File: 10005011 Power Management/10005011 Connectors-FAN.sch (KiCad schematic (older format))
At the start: 63 parts, among them IC25 L78M24CDT, IC6 TLV3012AIDBV, J10 BATTERY, J6 FAN, J7 CPU BOARD, J9 BLOWER, T23 IRLML2803, T31 IRLML5103

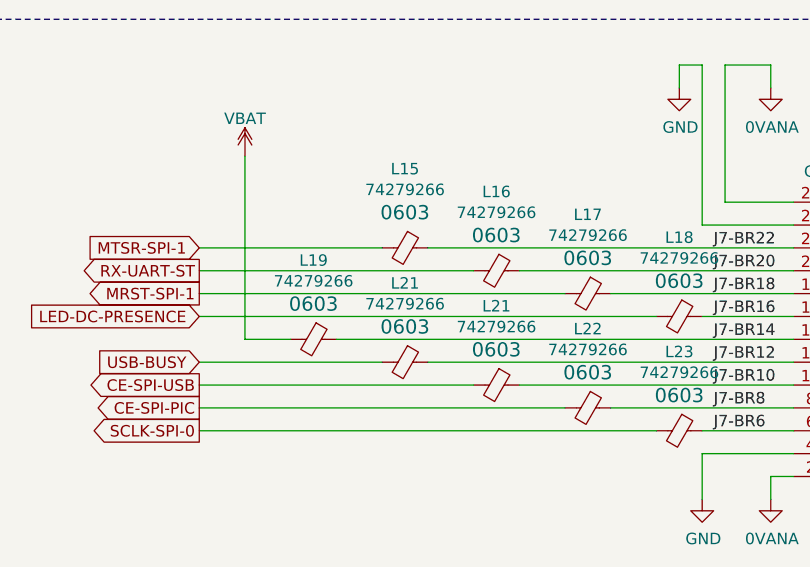
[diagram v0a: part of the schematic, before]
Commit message: solved repeated Res and Ind
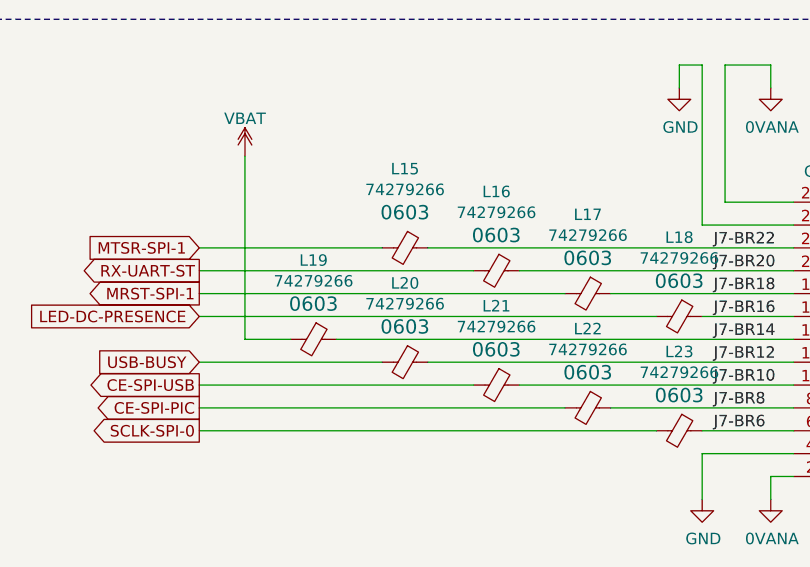
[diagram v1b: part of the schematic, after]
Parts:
- renumbered L21 to L20
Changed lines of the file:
@@
 $EndComp
 $Comp
-L 10005011_Power_Management_Schematic_Symbols:74279266 L21
+L 10005011_Power_Management_Schematic_Symbols:74279266 L20
 U 1 1 5EA74223
 P 6950 2850
-F 0 "L21" V 6605 2850 50  0000 C CNN
+F 0 "L20" V 6605 2850 50  0000 C CNN
 F 1 "74279266" V 6696 2850 50  0000 C CNN
 F 2 "10005011 Power Management:C0603_1" V 6880 2850 50  0001 C CNN

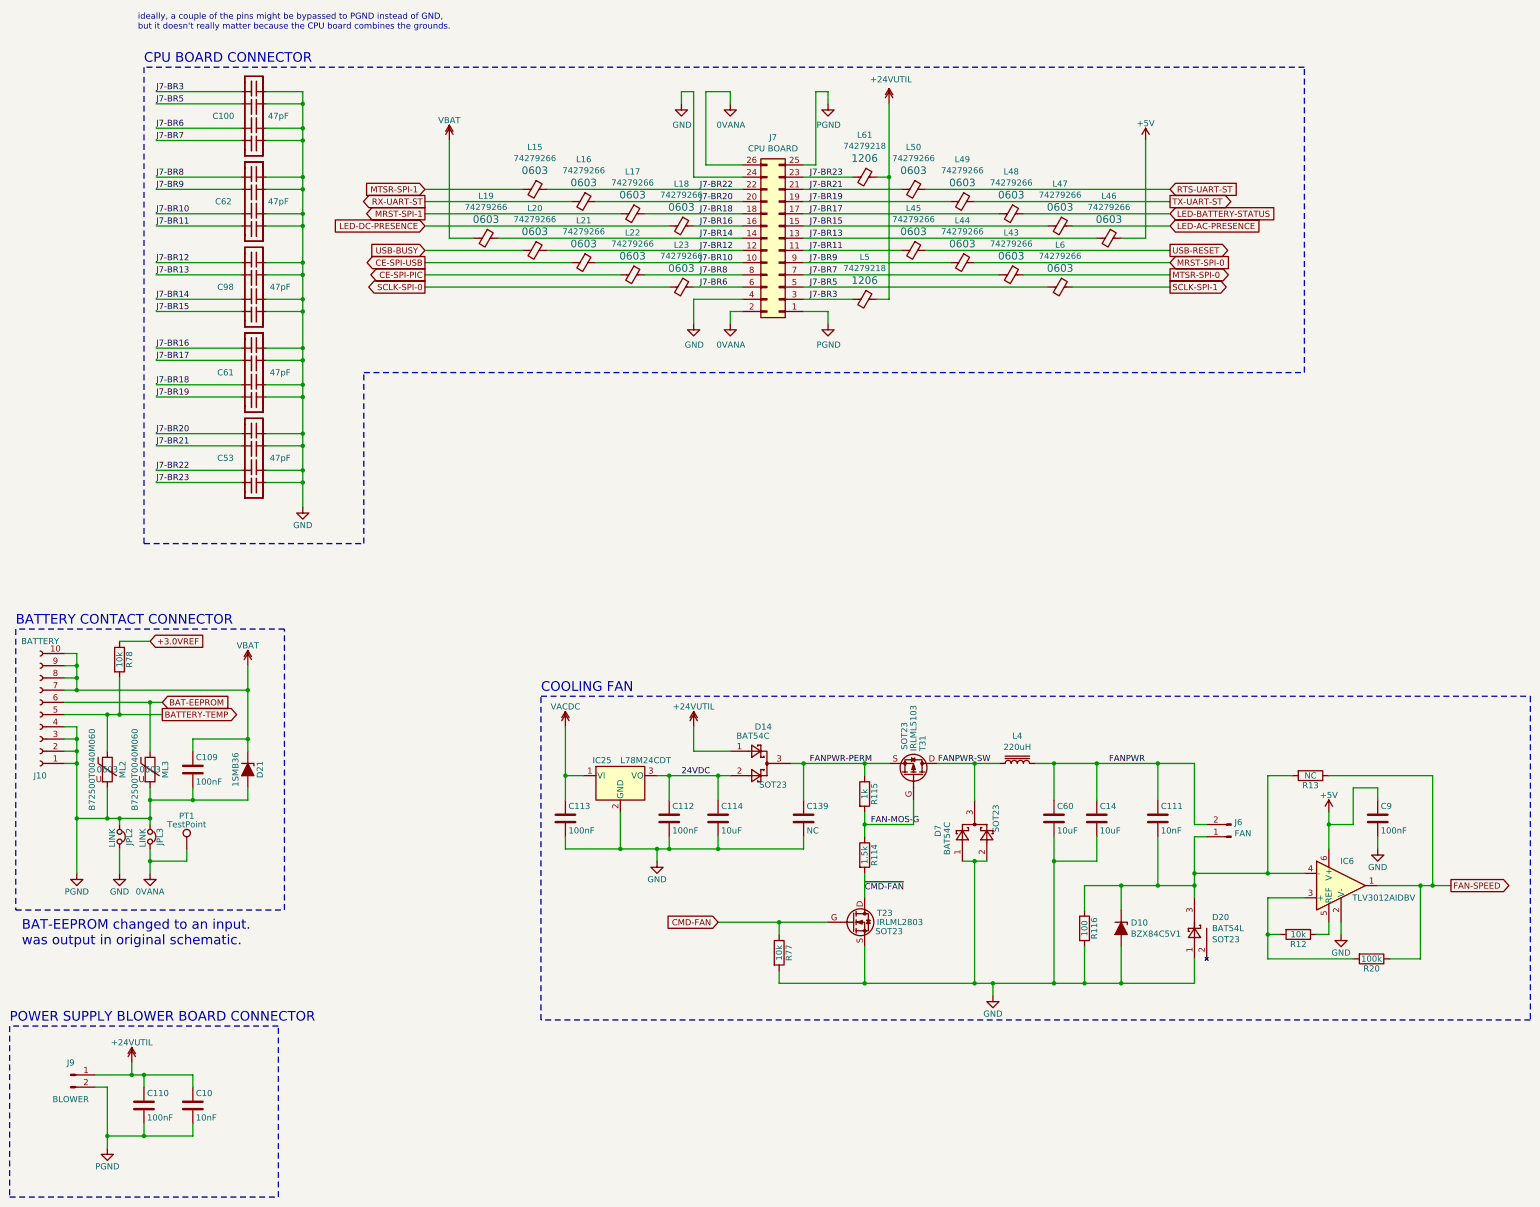
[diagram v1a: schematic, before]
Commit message: Powermanagement dev sheet4
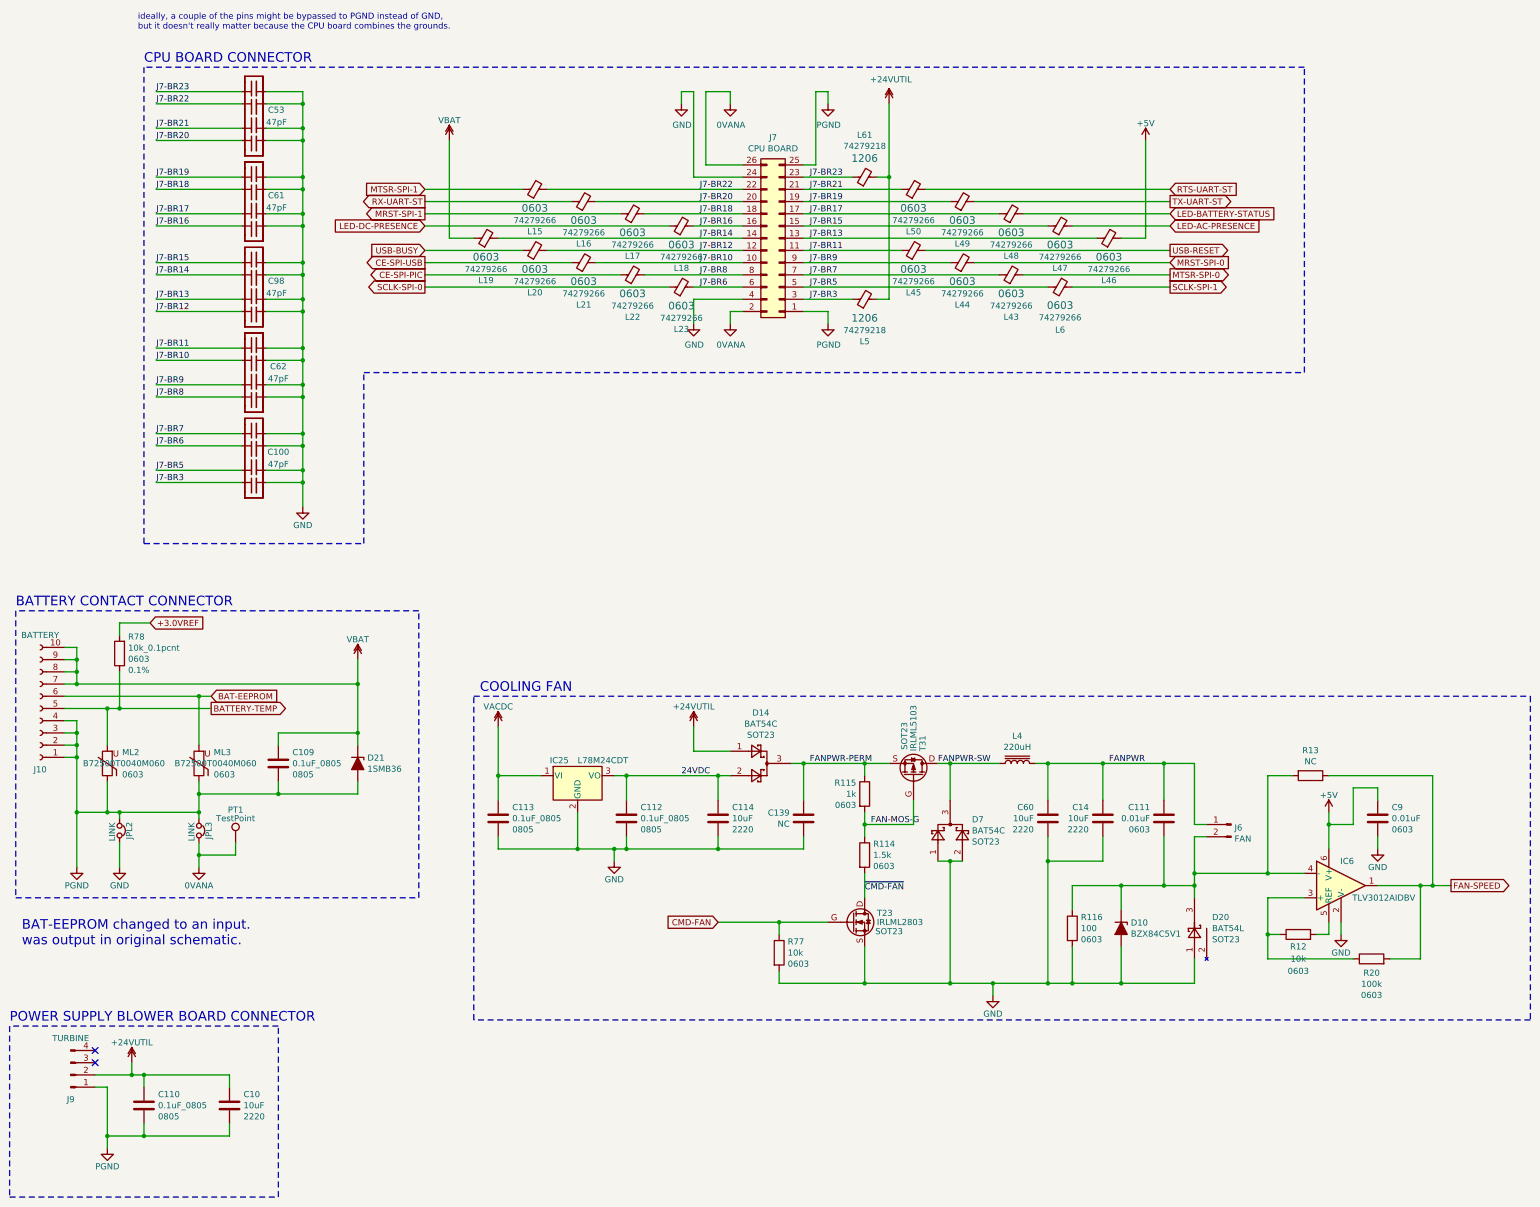
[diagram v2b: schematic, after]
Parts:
- removed C10: 10nF, 10005011 Power Management:C2220_1, symbol Device:C
- removed C109, C110, C112, C113: 100nF, 10005011 Power Management:C0805_1, symbol Device:C
- removed C111: 10nF, 10005011 Power Management:C0603_1, symbol Device:C
- removed C114, C14, C60: 10uF, 10005011 Power Management:C2220_1, symbol Device:C
- removed C9: 100nF, 10005011 Power Management:C0402_1, symbol Device:C
- removed J9: BLOWER, 10005011 Power Management:MOL43650-02D_1, symbol Connector:Conn_01x02_Male
- removed R114: 1.5k, 10005011 Power Management:RC1206_1, symbol Device:R
- removed R115: 1k, 10005011 Power Management:RC1206_1, symbol Device:R
- removed R116: 100, 10005011 Power Management:RC1206_1, symbol Device:R
- removed R12, R77, R78: 10k, 10005011 Power Management:R0603_1, symbol Device:R
- removed R20: 100k, 10005011 Power Management:R0603_1, symbol Device:R
- added C10, C114, C14, C60: 10uF, Capacitor_SMD:C_2220_5650Metric, symbol 10005011_Power_Management_Schematic_Symbols:10uF
- added C109, C110, C112, C113: 0.1uF_0805, Capacitor_SMD:C_0805_2012Metric, symbol 10005011_Power_Management_Schematic_Symbols:0.1uF_0805
- added C111, C9: 0.01uF, Capacitor_SMD:C_0603_1608Metric, symbol 10005011_Power_Management_Schematic_Symbols:0.01uF
- added J9: TURBINE, symbol Connector:Conn_01x04_Male
- added R114: 1.5k, Resistor_SMD:R_0603_1608Metric, symbol 10005011_Power_Management_Schematic_Symbols:1.5k
- added R115: 1k, Resistor_SMD:R_0603_1608Metric, symbol 10005011_Power_Management_Schematic_Symbols:1k
- added R116: 100, Resistor_SMD:R_0603_1608Metric, symbol 10005011_Power_Management_Schematic_Symbols:100
- added R12, R77: 10k, Resistor_SMD:R_0603_1608Metric, symbol 10005011_Power_Management_Schematic_Symbols:10k
- added R20: 100k, Resistor_SMD:R_0603_1608Metric, symbol 10005011_Power_Management_Schematic_Symbols:100k
- added R78: 10k_0.1pcnt, Resistor_SMD:R_0603_1608Metric, symbol 10005011_Power_Management_Schematic_Symbols:10k_0.1pcnt
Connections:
- net +24VUTIL: now also L5.2, L61.2, C10.2, C110.2, J9.2 (Pin_2); no longer L5.1, L61.1
- net +3.0VREF: now also R78.2
- net +5V: now also L46.2, C9.1; no longer L46.1
- net 24VDC: now also C112.2, C114.2
- net BAT-EEPROM: now also ML3.2; no longer ML3.1
- net BATTERY-TEMP: now also ML2.2, R78.1; no longer ML2.1
- net CE-SPI-PIC: now also L22.1; no longer L22.2
- net CE-SPI-USB: now also L21.1; no longer L21.2
- net CMD-FAN: now also R77.1
- net FAN-MOS-G: now also R114.1, R115.2
- net FAN-SPEED: now also R20.2
- net FANPWR: now also J6.1 (Pin_1), C111.2, C14.2, C60.2; no longer J6.2 (Pin_2)
- net FANPWR-PERM: now also C139.2, R115.1; no longer C139.1
- net GND: now also C100.1, C100.2, C100.3, C100.4, C139.1, C53.1, C53.2, C53.3, C53.4, C61.1, C61.2, C61.3, C61.4, C62.1, C62.2, C62.3, C62.4, C98.1, C98.2, C98.3, C98.4, C112.1, C113.1, C114.1, C14.1, C60.1, C9.2, R116.2, R77.2; no longer C100.5, C100.6, C100.7, C100.8, C139.2, C53.5, C53.6, C53.7, C53.8, C61.5, C61.6, C61.7, C61.8, C62.5, C62.6, C62.7, C62.8, C98.5, C98.6, C98.7, C98.8
- net J7-BR10: now also C62.6, L21.2; no longer C62.3, L21.1
- net J7-BR11: now also C62.5, L45.1; no longer C62.4, L45.2
- net J7-BR12: now also C98.8, L20.2; no longer C98.1, L20.1
- net J7-BR13: now also C98.7, L46.1; no longer C98.2, L46.2
- net J7-BR14: now also C98.6, L19.2; no longer C98.3, L19.1
- net J7-BR15: now also C98.5, L47.1; no longer C98.4, L47.2
- net J7-BR16: now also C61.8, L18.2; no longer C61.1, L18.1
- net J7-BR17: now also C61.7, L48.1; no longer C61.2, L48.2
- net J7-BR18: now also C61.6, L17.2; no longer C61.3, L17.1
- net J7-BR19: now also C61.5, L49.1; no longer C61.4, L49.2
- net J7-BR20: now also C53.8, L16.2; no longer C53.1, L16.1
- net J7-BR21: now also C53.7, L50.1; no longer C53.2, L50.2
- net J7-BR22: now also C53.6, L15.2; no longer C53.3, L15.1
- net J7-BR23: now also C53.5, L61.1; no longer C53.4, L61.2
- net J7-BR3: now also C100.8, L5.1; no longer C100.1, L5.2
- net J7-BR5: now also C100.7; no longer C100.2
- net J7-BR6: now also C100.6, L23.2; no longer C100.3, L23.1
- net J7-BR7: now also C100.5, L43.1; no longer C100.4, L43.2
- net J7-BR8: now also C62.8, L22.2; no longer C62.1, L22.1
- net J7-BR9: now also C62.7, L44.1; no longer C62.2, L44.2
- net LED-AC-PRESENCE: now also L47.2; no longer L47.1
- net LED-BATTERY-STATUS: now also L48.2; no longer L48.1
- net LED-DC-PRESENCE: now also L18.1; no longer L18.2
- net MRST-SPI-0: now also L44.2; no longer L44.1
- net MRST-SPI-1: now also L17.1; no longer L17.2
- net MTSR-SPI-0: now also L43.2; no longer L43.1
- net MTSR-SPI-1: now also L15.1; no longer L15.2
- net PGND: now also ML2.1, ML3.1, C10.1, C109.1, C110.1, J9.1 (Pin_1); no longer ML2.2, ML3.2
- net RTS-UART-ST: now also L50.2; no longer L50.1
- net RX-UART-ST: now also L16.1; no longer L16.2
- net SCLK-SPI-0: now also L23.1; no longer L23.2
- net TX-UART-ST: now also L49.2; no longer L49.1
- net USB-BUSY: now also L20.1; no longer L20.2
- net USB-RESET: now also L45.2; no longer L45.1
- net VACDC: now also C113.2
- net VBAT: now also L19.1, C109.2; no longer L19.2
- net ~CMD-FAN: now also R114.2
- net at IC6.3 (+): now also R12.1, R20.1
- net at D10.K, D20.3, IC6.4 (-)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: now also J6.2 (Pin_2), C111.1, R116.1; no longer J6.1 (Pin_1)
- net at IC6.5 (REF): now also R12.2
- no-connect marks 0 -> 2
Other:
- moved on the sheet: C100, C53, C61, C62, D21, D7, IC25, J10, JPL2, JPL3, ML2, ML3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

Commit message: Powermanagement dev netlist fix
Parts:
- J9: footprint (none) -> 10005011 Power Management:MOL43650-02D_1; Description (none) -> CONNECTOR MICRO-FIT, 2 CIRCUITS,3MM,5A,250V; Item Number (none) -> 10022874; Manufacturer (none) -> MOLEX; Manufacturer_No (none) -> 43650-0224
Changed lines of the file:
@@
 F 0 "J9" H 3150 9800 50  0000 C CNN
 F 1 "TURBINE" H 3150 9300 50  0000 C CNN
-F 2 "" H 3150 9600 50  0001 C CNN
+F 2 "10005011 Power Management:MOL43650-02D_1" H 3150 9600 50  0001 C CNN
 F 3 "~" H 3150 9600 50  0001 C CNN
+F 4 "CONNECTOR MICRO-FIT, 2 CIRCUITS,3MM,5A,250V" H 3150 9600 50  0001 C CNN "Description"
+F 5 "10022874" H 3150 9600 50  0001 C CNN "Item Number"
+F 6 "MOLEX" H 3150 9600 50  0001 C CNN "Manufacturer"
+F 7 "43650-0224" H 3150 9600 50  0001 C CNN "Manufacturer_No"
 	1    3150 9600
 	1    0    0    1

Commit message: Powermanagement dev library
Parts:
- C10, C114, C14, C60: footprint Capacitor_SMD:C_2220_5650Metric -> 10005011 Power Management:C2220_1; symbol 10005011_Power_Management_Schematic_Symbols:10uF -> Device:C; Bom_Footprint 2220 -> (none); Description CAP CER 10UF 50V X7R 2220 -> CAPACITOR CERAMIC, 10UF,+/-10%,50V; Item Number (none) -> 10039581; Manufacturer (none) -> AVX; Manufacturer_No (none) -> 22205C106K4Z4A
- C100, C61, C62, C98: symbol 10005011_Power_Management_Schematic_Symbols:47pF_array -> 10005011_Power_Management:47pF_array; Description CAP ARRAY 47PF 50V NP0 0612 -> CAPACITOR ARRAY, 47PF, 50V, +/-10%,NPO,0612; Dielectric NPO -> (none); Item Number (none) -> 10022136; Notes Need to create a footprint -> (none); Voltage 50V -> (none)
- C109, C110, C112, C113: value 0.1uF_0805 -> 100nF; footprint Capacitor_SMD:C_0805_2012Metric -> 10005011 Power Management:C0805_1; symbol 10005011_Power_Management_Schematic_Symbols:0.1uF_0805 -> Device:C; Bom_Footprint 0805 -> (none); Description CAP CER 0.1UF 50V X7R 0805 -> CAPACITOR CERAMIC, 100NF, +/-10%, 50V, X7R,0805; Item Number (none) -> 10022135
- C111, C9: footprint Capacitor_SMD:C_0603_1608Metric -> 10005011 Power Management:C0603_1; symbol 10005011_Power_Management_Schematic_Symbols:0.01uF -> Device:C
- C53: symbol 10005011_Power_Management_Schematic_Symbols:47pF_array -> 10005011_Power_Management:47pF_array; Description CAP ARRAY 47PF 50V NP0 0612 -> CAPACITOR ARRAY, 47PF, 50V, +/-10%,NPO,0612; Item Number (none) -> 10022136
- D10: symbol 10005011_Power_Management_Schematic_Symbols:BZX84C5V1 -> 10005011_Power_Management:BZX84C5V1; Description DIODE ZENER 5.1V 300MW SOT23-3 -> DIODE ZENER, 0.35,5.1V, SOT23; Item Number (none) -> 10022657
- D14, D7: symbol 10005011_Power_Management_Schematic_Symbols:BAT54C -> 10005011_Power_Management:BAT54C; BOM_Footprint SOT23 -> (none); Item Number (none) -> 10022653
- D20: value BAT54L -> BAT54; symbol 10005011_Power_Management_Schematic_Symbols:BAT54L -> 10005011_Power_Management:BAT54; BOM_Footprint SOT23 -> (none); Item Number (none) -> 10022652
- D21: symbol 10005011_Power_Management_Schematic_Symbols:SZ1SMB -> 10005011_Power_Management:SZ1SMB; Item Number (none) -> 10022654
- IC6: symbol pages_4-5:TLV3012AIDBV -> 10005011_Power_Management:TLV3012AIDBV; Description (none) -> IC, COMPARATOR, SOT23-6; Item Number (none) -> 10022739; Manufacturer (none) -> TEXAS INSTRUMENTS; Manufacturer_No (none) -> TLV3012AIDBVR
- L15, L16, L17, L18, L19, L20, L21, L22, L23, L43, L44, L45, L46, L47, L48, L49, L50, L6: symbol 10005011_Power_Management_Schematic_Symbols:74279266 -> Device:Ferrite_Bead_Small; Bom_Footprint 0603 -> (none); Item Number (none) -> 10022907
- L5: symbol 10005011_Power_Management_Schematic_Symbols:74279218 -> Device:Ferrite_Bead_Small; Description FERRITE BEAD 600 OHM 1206 1LN -> SMD FERRITE, 1A,1206; Item Number (none) -> 10022911
- L61: symbol 10005011_Power_Management_Schematic_Symbols:74279218 -> Device:Ferrite_Bead_Small; Bom_Footprint 1206 -> (none); Item Number (none) -> 10022911
- ML2, ML3: symbol 10005011_Power_Management_Schematic_Symbols:B72500T0040M060 -> Device:Varistor; Bom_Footprint 0603 -> (none); Description VARISTOR 8V 30A 0603 -> SMD VARISTOR, 5.5V,C0603; Item Number (none) -> 10022926
- R114: footprint Resistor_SMD:R_0603_1608Metric -> 10005011 Power Management:R0603_1; symbol 10005011_Power_Management_Schematic_Symbols:1.5k -> Device:R
- R115: footprint Resistor_SMD:R_0603_1608Metric -> 10005011 Power Management:R0603_1; symbol 10005011_Power_Management_Schematic_Symbols:1k -> Device:R
- R116: footprint Resistor_SMD:R_0603_1608Metric -> 10005011 Power Management:R0603_1; symbol 10005011_Power_Management_Schematic_Symbols:100 -> Device:R
- R12, R77: footprint Resistor_SMD:R_0603_1608Metric -> 10005011 Power Management:R0603_1; symbol 10005011_Power_Management_Schematic_Symbols:10k -> Device:R
- R20: footprint Resistor_SMD:R_0603_1608Metric -> 10005011 Power Management:R0603_1; symbol 10005011_Power_Management_Schematic_Symbols:100k -> Device:R
- R78: value 10k_0.1pcnt -> 10k; footprint Resistor_SMD:R_0603_1608Metric -> 10005011 Power Management:R0603_1; symbol 10005011_Power_Management_Schematic_Symbols:10k_0.1pcnt -> Device:R; Bom_Footprint 0603 -> (none); Description RES SMD 10K OHM 0.1% 1/10W 0603 -> RESISTOR, PRECISION,10K OHM, 0.063W,+/-0.1%,0603; Item Number (none) -> 10022701; Tolerance 0.1% -> (none); Wattage 1/10W -> (none)
- T23: symbol 10005011_Power_Management_Schematic_Symbols:IRLML2803TRPBF -> 10005011_Power_Management:IRLML2803TRPBF; Bom_Footprint SOT23 -> (none); Description MOSFET N-CH 30V 1.2A SOT-23 -> TRANSISTOR MOSFET, 30V, 0.93A, 0.25 OHM, N CHANNEL; Item Number (none) -> 10022558
- T31: symbol 10005011_Power_Management_Schematic_Symbols:IRLML5103TRPBF -> 10005011_Power_Management:IRLML5103TRPBF; Bom_Footprint SOT23 -> (none); Item Number (none) -> 10022933
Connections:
- net +24VUTIL: now also C110.1; no longer C110.2
- net PGND: now also C110.2; no longer C110.1
